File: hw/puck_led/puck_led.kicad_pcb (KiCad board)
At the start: 2 copper layers, 8 x 37 mm, 11 parts

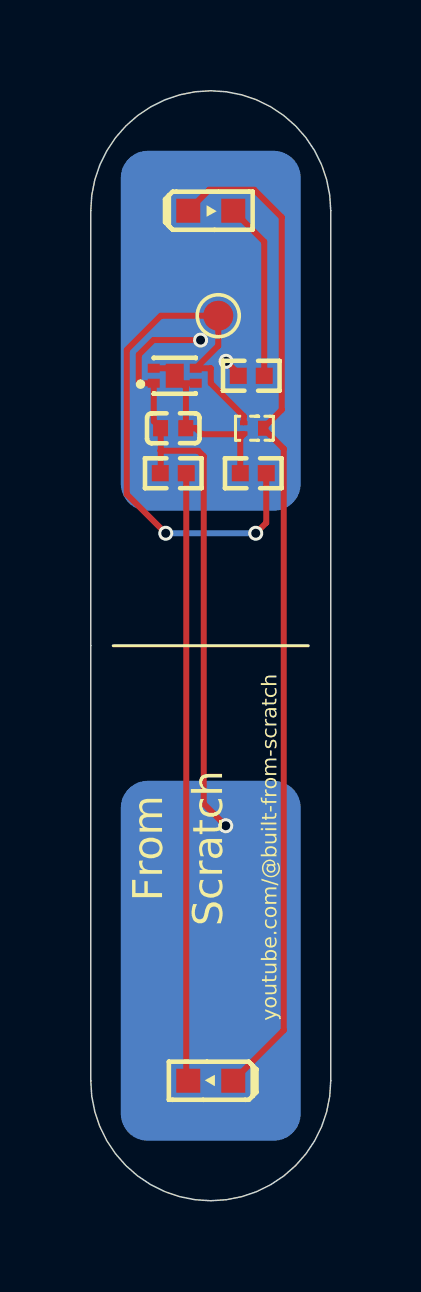
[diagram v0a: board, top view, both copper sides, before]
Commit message: Added test mode
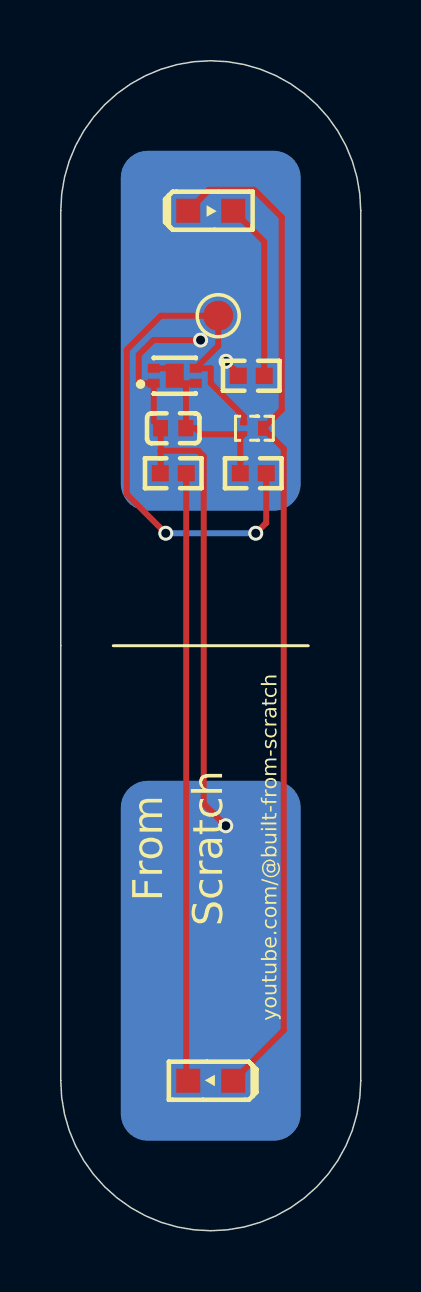
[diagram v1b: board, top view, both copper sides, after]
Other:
- board size 8 x 37 mm -> 10 x 39 mm
